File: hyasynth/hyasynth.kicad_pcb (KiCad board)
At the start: 2 copper layers, 102 x 50 mm, 37 parts, among them J1 Conn_01x04_Male, J2 Conn_01x02_Male, J3 Conn_01x07_Male, J4 Conn_01x02_Male, J5 Conn_01x02_Male, SW1 Power Switch, SW10 G# Ab, SW11 A, SW12 A# Bb, SW13 B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

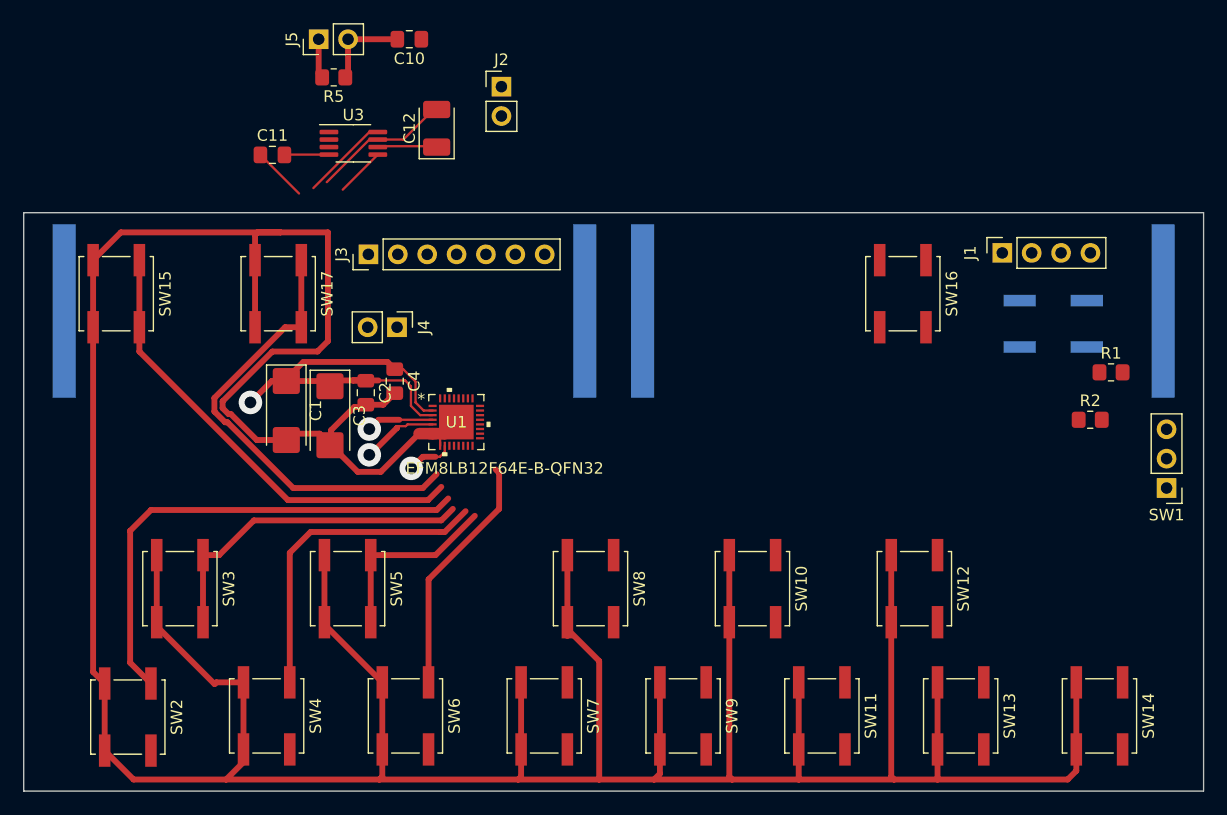
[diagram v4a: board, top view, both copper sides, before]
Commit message: wired in switches and dac mostly
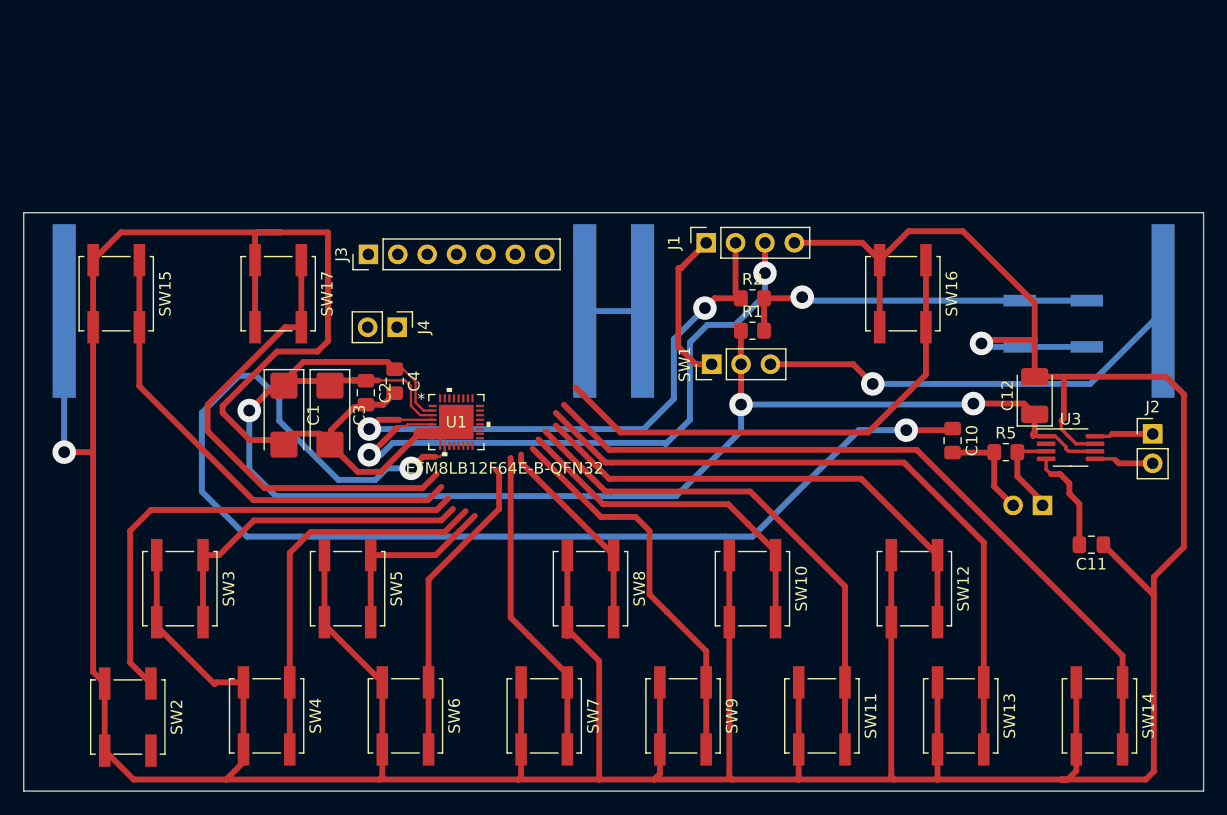
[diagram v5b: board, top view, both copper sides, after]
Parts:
- J5: moved to B.Cu
- moved C11 78.4 mm to (251.5, 58.9), turned to 180 degrees
- moved J5 74.4 mm to (247.3, 55.5)
- moved U3 67.3 mm to (249.7, 50.5)
- moved R5 66.5 mm to (244.1, 50.9), turned to 0 degrees
- moved J2 63.8 mm to (256.8, 49.3)
- moved C10 58.4 mm to (239.5, 49.9), turned to -90 degrees
- moved C12 56.6 mm to (246.6, 46.0)
- moved SW1 40.8 mm to (218.7, 43.3), turned to 90 degrees
- moved R1 31.2 mm to (222.2, 40.4)
- moved R2 31.0 mm to (222.2, 37.6)
- moved J1 25.6 mm to (218.2, 32.8)
- moved C1 0.45 mm to (181.7, 47.7)
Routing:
- net GND: track 381.2 -> 500.2 mm, vias 0 -> 2
- net /DAC: track 4.14 -> 106.0 mm, vias 1 -> 2
- net VDD: track 40.7 -> 129.7 mm, vias 1 -> 3
- net /C: track 0.00 -> 65.4 mm
- net /B: track 0.00 -> 59.5 mm
- net /C2D: track 6.56 -> 55.2 mm, vias 1 -> 2
- net /A: track 0.00 -> 45.6 mm
- net /C2CLK: track 5.81 -> 50.6 mm, vias 1 -> 2
- net /Function: track 0.00 -> 43.9 mm
- net /A#: track 0.00 -> 43.4 mm
- net Net-(BT1-Pad1): track 0.00 -> 37.3 mm, vias 0 -> 1
- net /G: track 0.00 -> 34.0 mm
- net Net-(R1-Pad2): track 0.00 -> 30.9 mm, vias 0 -> 1
- net /G#: track 0.00 -> 30.6 mm
- net /F: track 0.00 -> 27.2 mm
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
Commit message: finished pcb v1
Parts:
- moved J4 4.08 mm to (187.5, 41.0), turned to 180 degrees
- moved C1 1.71 mm to (180.0, 47.5)
- moved C3 1.69 mm to (184.0, 47.5)
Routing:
- net /DAC: track 106.0 -> 52.4 mm
- net VDD: track 129.7 -> 146.7 mm
- net /GPIO_0: track 0.00 -> 15.6 mm
- net /GPIO_4: track 0.00 -> 15.5 mm
- net /Uart_RX: track 0.00 -> 14.5 mm
- net /GPIO_3: track 0.00 -> 14.0 mm
- net /Uart_TX: track 0.00 -> 13.6 mm
- net /GPIO_2: track 0.00 -> 13.1 mm
- net /GPIO_1: track 0.00 -> 12.8 mm
- net /Up: track 41.3 -> 53.8 mm
- net /Low_C: track 42.6 -> 54.3 mm
- net /C: track 65.4 -> 74.3 mm
- net /D#: track 16.2 -> 25.0 mm
- net /D: track 33.7 -> 41.4 mm
- net /C#: track 29.1 -> 36.4 mm
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- added copper zone on B.Cu, net GND
- added copper zone on F.Cu, net GND
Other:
- board size 102 x 50 mm -> 108 x 53 mm

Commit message: final first draft I swear
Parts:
- moved SW1 1.10 mm to (218.8, 44.4)
- moved J4 0.96 mm to (186.6, 40.7)
- turned SW17 to -90 degrees
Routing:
- net GND: track 498.4 -> 491.4 mm
- net /Up: track 53.8 -> 47.8 mm
- net /Debug_Power: track 13.5 -> 15.0 mm
- net Net-(BT1-Pad1): track 35.9 -> 37.0 mm

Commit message: borrowed new button footprint
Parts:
- SW14: footprint Button_Switch_SMD:SW_Push_1P1T_NO_CK_KSC7xxJ -> button:SW_Push_hand_solder
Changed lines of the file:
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@@
     (pad_to_mask_clearance 0)
     (pcbplotparams
-      (layerselection 0x0001000_7fffffff)
+      (layerselection 0x000103c_ffffffff)
       (disableapertmacros false)
       (usegerberextensions false)
@@
       (drillshape 0)
       (scaleselection 1)
-      (outputdirectory "./")
+      (outputdirectory "/home/angus/OneDrive/Work/4th year/eetp/hyasynth-pcb/fab/")
     )
   )
@@
     )
   )
-  (footprint "Button_Switch_SMD:SW_Push_1P1T_NO_CK_KSC7xxJ" locked (layer "F.Cu")
+  (footprint "button:SW_Push_hand_solder" locked (layer "F.Cu")
     (at 252.2 73.7 90)
     (descr "CK components KSC7 tactile switch https://www.ckswitches.com/media/1973/ksc7.pdf")
@@
     (property "Sheetname" "")
     (attr smd)
-    (fp_text reference "SW14" (at 0 4.24 90) (layer "F.SilkS")
-      (effects (font (size 1 1) (thickness 0.15)))
-    )
-    (fp_text value "C" (at 0 -4.23 90) (layer "F.Fab")
+    (fp_text reference "SW14" (at 0 4.5 90) (layer "F.SilkS")
+      (effects (font (size 1 1) (thickness 0.15)))
+    )
+    (fp_text value "C" (at 0 -6 90) (layer "F.Fab")
       (effects (font (size 1 1) (thickness 0.15)))
     )
@@
       (effects (font (size 1 1) (thickness 0.15)))
     )
-    (fp_line (start 3.21 3.21) (end 3.21 2.93) (layer "F.SilkS") (width 0.12))
-    (fp_line (start -3.21 2.8) (end -3.21 3.21) (layer "F.SilkS") (width 0.12))
-    (fp_line (start 3.21 1.2) (end 3.21 -1.2) (layer "F.SilkS") (width 0.12))
-    (fp_line (start 3.21 -2.8) (end 3.21 -3.21) (layer "F.SilkS") (width 0.12))
-    (fp_line (start -3.21 3.21) (end 3.21 3.21) (layer "F.SilkS") (width 0.12))
-    (fp_line (start 3.21 -3.21) (end -3.21 -3.21) (layer "F.SilkS") (width 0.12))
-    (fp_line (start -3.21 -3.21) (end -3.21 -2.8) (layer "F.SilkS") (width 0.12))
-    (fp_line (start -3.21 -1.2) (end -3.21 1.2) (layer "F.SilkS") (width 0.12))
+    (fp_line (start 4.55 3.35) (end -4.55 3.35) (layer "F.CrtYd") (width 0.05))
+    (fp_line (start 4.55 -3.35) (end 4.55 3.35) (layer "F.CrtYd") (width 0.05))
     (fp_line (start -4.55 3.35) (end -4.55 -3.35) (layer "F.CrtYd") (width 0.05))
-    (fp_line (start 4.55 -3.35) (end 4.55 3.35) (layer "F.CrtYd") (width 0.05))
-    (fp_line (start 4.55 3.35) (end -4.55 3.35) (layer "F.CrtYd") (width 0.05))
     (fp_line (start -4.55 -3.35) (end 4.55 -3.35) (layer "F.CrtYd") (width 0.05))
-    (fp_line (start -3.1 3.1) (end -3.1 -3.1) (layer "F.Fab") (width 0.1))
-    (fp_line (start 3.1 -3.1) (end 3.1 3.1) (layer "F.Fab") (width 0.1))
+    (fp_line (start -3.1 3.5) (end -3.1 -3.1) (layer "F.Fab") (width 0.1))
+    (fp_line (start 3.1 3.5) (end -3.1 3.5) (layer "F.Fab") (width 0.1))
     (fp_line (start -3.1 -3.1) (end 3.1 -3.1) (layer "F.Fab") (width 0.1))
-    (fp_line (start 3.1 3.1) (end -3.1 3.1) (layer "F.Fab") (width 0.1))
+    (fp_line (start 3.1 -3.1) (end 3.1 3.5) (layer "F.Fab") (width 0.1))
     (fp_circle (center 0 0) (end 1.5 0) (layer "F.Fab") (width 0.1) (fill none))
-    (pad "1" smd rect locked (at -2.9 -2 90) (size 2.8 1) (layers "F.Cu" "F.Paste" "F.Mask")
-      (net 3 "GND") (pinfunction "1") (pintype "passive"))
-    (pad "1" smd rect locked (at 2.9 -2 90) (size 2.8 1) (layers "F.Cu" "F.Paste" "F.Mask")
-      (net 3 "GND") (pinfunction "1") (pintype "passive"))
-    (pad "2" smd rect locked (at -2.9 2 90) (size 2.8 1) (layers "F.Cu" "F.Paste" "F.Mask")
+    (pad "1" smd rect locked (at -5 -2.25 90) (size 2.8 1.6) (layers "F.Cu" "F.Paste" "F.Mask")
+      (net 3 "GND") (pinfunction "1") (pintype "passive"))
+    (pad "1" smd rect locked (at 5 -2.25 90) (size 2.8 1.6) (layers "F.Cu" "F.Paste" "F.Mask")
+      (net 3 "GND") (pinfunction "1") (pintype "passive"))
+    (pad "2" smd rect locked (at -5 2.25 90) (size 2.8 1.6) (layers "F.Cu" "F.Paste" "F.Mask")
       (net 19 "/C") (pinfunction "2") (pintype "passive"))
-    (pad "2" smd rect locked (at 2.9 2 90) (size 2.8 1) (layers "F.Cu" "F.Paste" "F.Mask")
+    (pad "2" smd rect locked (at 5 2.25 90) (size 2.8 1.6) (layers "F.Cu" "F.Paste" "F.Mask")
       (net 19 "/C") (pinfunction "2") (pintype "passive"))
     (model "${KICAD6_3DMODEL_DIR}/Button_Switch_SMD.3dshapes/SW_push_1P1T_NO_CK_KSC7xxJxxx.wrl"
